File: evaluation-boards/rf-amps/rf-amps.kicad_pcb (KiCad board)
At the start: 4 copper layers, 23 x 37 mm, 22 parts, among them J1 Conn_01x02, J2 Conn_01x02, J3 CONN_01X03, J4 CONN_COAXIAL, J5 CONN_COAXIAL, J6 CONN_COAXIAL, J7 CONN_COAXIAL, U1 BGB741L7ESD

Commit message: Update rf-amps board
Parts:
- removed C5, C6: 100nF, gsg-modules:0402
- removed C7, C8: 1uF, gsg-modules:0603
- removed J6, J7: CONN_COAXIAL, gsg-modules:SMA-73251-2120
- C1, C2, C9: value 100nF -> 1uF; footprint gsg-modules:0402 -> Capacitor_SMD:C_0201_0603Metric
- C3, C4: footprint gsg-modules:0603 -> Capacitor_SMD:C_0201_0603Metric
- J4, J5: footprint gsg-modules:SMA-73251-2120 -> sma-variants:Linx_SMA_CONSMA003.062
- L1, L2: value 10uH -> 47uH; footprint gsg-modules:0603 -> Inductor_SMD:L_0603_1608Metric
- L3, L4: value 10uH -> 33nH; footprint gsg-modules:0603 -> Inductor_SMD:L_0201_0603Metric
- R1: footprint gsg-modules:0603 -> Resistor_SMD:R_0402_1005Metric
- moved L4 16.9 mm to (145.1, 80.3)
- moved L3 15.7 mm to (138.5, 79.7)
- moved C4 8.54 mm to (141.3, 81.3)
- moved L2 4.36 mm to (143.2, 81.3), turned to 180 degrees
- moved L1 4.11 mm to (138.4, 78.2), turned to 0 degrees
- moved C1 3.16 mm to (137.1, 80.0)
- moved C2 3.16 mm to (146.5, 80.0)
- moved J1 3.16 mm to (138.0, 67.6)
- moved J2 3.16 mm to (132.9, 67.6)
- moved J3 3.16 mm to (143.1, 67.6)
- moved J4 3.16 mm to (130.0, 80.0)
- moved J5 3.16 mm to (153.0, 80.0)
- moved R1 3.11 mm to (143.9, 77.3)
- moved U1 3.04 mm to (142.0, 79.5)
- moved C9 2.21 mm to (141.4, 78.3), turned to 180 degrees
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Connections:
- C1 pad 1: Net-(C1-Pad1) -> Net-(U1-RFIN)
- C2 pad 2: Net-(C2-Pad2) -> Net-(U1-RFOUT)
- L1 pad 1: Net-(C1-Pad1) -> Net-(L1-Pad1)
- L2 pad 1: Net-(C2-Pad2) -> Net-(L2-Pad1)
- L3 pad 1: Net-(C5-Pad1) -> Net-(U1-RFIN)
- L3 pad 2: Net-(C7-Pad2) -> Net-(L1-Pad1)
- L4 pad 1: Net-(C5-Pad1) -> Net-(U1-RFOUT)
- L4 pad 2: VCC -> Net-(L2-Pad1)
- U1 pad 3: Net-(C1-Pad1) -> Net-(U1-RFIN)
- U1 pad 4: Net-(C2-Pad2) -> Net-(U1-RFOUT)
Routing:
- net Net-(C5-Pad1): track 8.83 -> 0.00 mm
- net VCC: track 9.74 -> 3.57 mm, vias 4 -> 3
- net Net-(C5-Pad2): track 4.37 -> 0.00 mm
- net GND: track 6.49 -> 2.41 mm, vias 5 -> 3
- net Net-(C6-Pad1): track 3.87 -> 0.00 mm
- net Net-(C1-Pad1): track 3.70 -> 0.00 mm
- net Net-(C2-Pad2): track 3.50 -> 0.00 mm
- net Net-(U1-RFIN): track 0.00 -> 3.40 mm
- net Net-(U1-RFOUT): track 0.00 -> 3.00 mm
- net Net-(U1-BIAS): track 4.04 -> 2.21 mm
- net Net-(C7-Pad2): track 1.75 -> 0.00 mm
- net Net-(L1-Pad1): track 0.00 -> 1.55 mm
- net Net-(L2-Pad1): track 0.00 -> 1.39 mm
- net Net-(J3-Pin_2): track 12.8 -> 13.5 mm
- net Net-(U1-ADJ): track 2.40 -> 1.87 mm
- added copper zone on In1.Cu, net GND
- added copper zone on In2.Cu, net VCC
- removed copper zone on C2.Cu, net GND
- removed copper zone on C3.Cu, net VCC
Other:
- net class Default removed
- board text added: "2024-11-04"
- board text added: "IN"
- board text added: "OUT"
- board text added: "rf-amps"
- board text removed: "12 August 2020"
- board text removed: "J4 IN"
- board text removed: "J5 OUT"

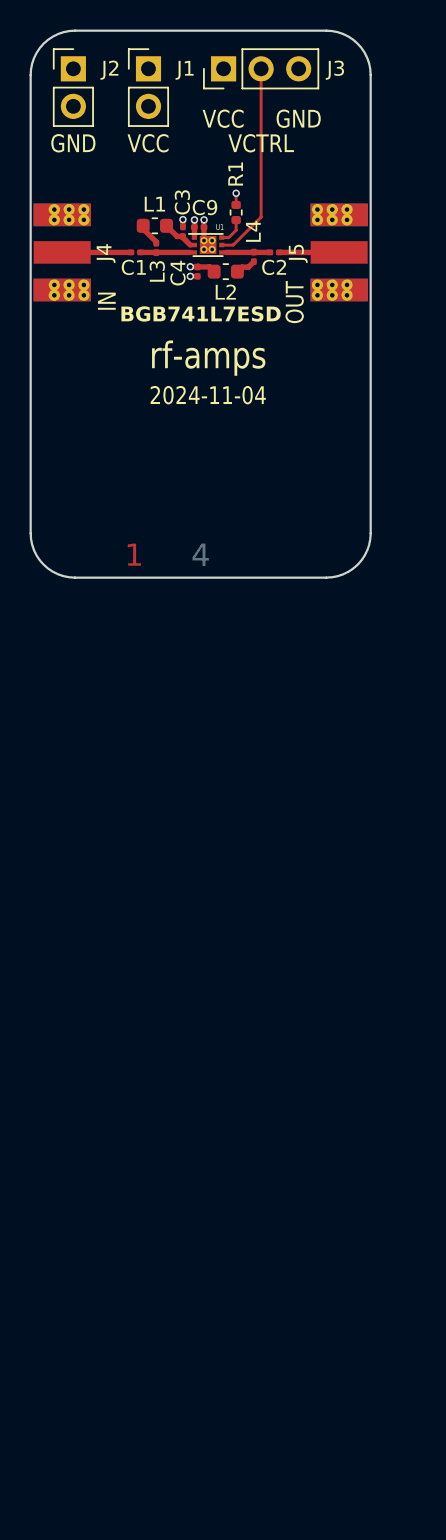
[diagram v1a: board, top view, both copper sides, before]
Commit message: Add more amplifiers to rf-amps board
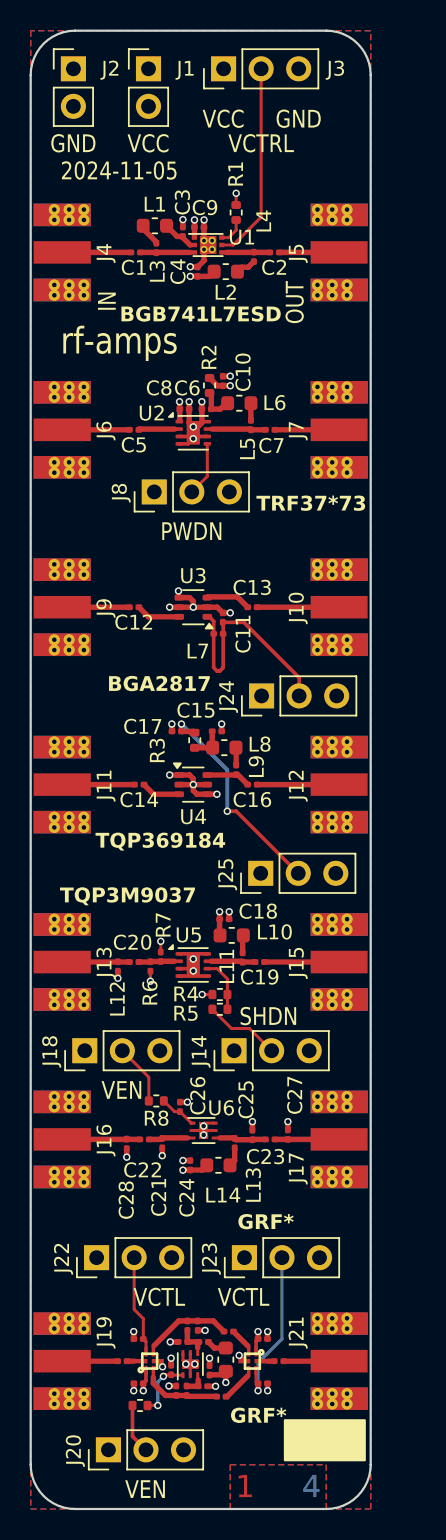
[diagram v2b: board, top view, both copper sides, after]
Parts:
- added C10: 1uF, Capacitor_SMD:C_0201_0603Metric, F.Cu at (143.0, 88.7)
- added C11: 1uF, Capacitor_SMD:C_0201_0603Metric, F.Cu at (143.0, 104.7)
- added C12: 1uF, Capacitor_SMD:C_0201_0603Metric, F.Cu at (137.0, 104.0)
- added C13: 1uF, Capacitor_SMD:C_0201_0603Metric, F.Cu at (145.0, 104.0)
- added C14: 1uF, Capacitor_SMD:C_0201_0603Metric, F.Cu at (137.3, 116.0)
- added C15: 1uF, Capacitor_SMD:C_0201_0603Metric, F.Cu at (142.6, 112.4)
- added C16: 1uF, Capacitor_SMD:C_0201_0603Metric, F.Cu at (145.0, 116.0)
- added C17: 1uF, Capacitor_SMD:C_0201_0603Metric, F.Cu at (139.9, 112.4)
- added C18: 1uF, Capacitor_SMD:C_0201_0603Metric, F.Cu at (143.1, 125.1)
- added C19: 1uF, Capacitor_SMD:C_0201_0603Metric, F.Cu at (145.5, 128.0)
- added C20: 1uF, Capacitor_SMD:C_0201_0603Metric, F.Cu at (137.0, 128.0)
- added C21: 0.2pF, Capacitor_SMD:C_0201_0603Metric, F.Cu at (138.9, 140.2)
- added C22: 1uF, Capacitor_SMD:C_0201_0603Metric, F.Cu at (137.7, 140.0)
- added C23: 1uF, Capacitor_SMD:C_0201_0603Metric, F.Cu at (146.2, 140.0)
- added C24: 1uF, Capacitor_SMD:C_0201_0603Metric, F.Cu at (140.8, 141.8)
- added C25: C, Capacitor_SMD:C_0201_0603Metric, F.Cu at (145.0, 139.7)
- added C26: 100pF, Capacitor_SMD:C_0201_0603Metric, F.Cu at (140.1, 137.8)
- added C27: C, Capacitor_SMD:C_0201_0603Metric, F.Cu at (147.4, 139.7)
- added C28: C, Capacitor_SMD:C_0201_0603Metric, F.Cu at (136.5, 140.3)
- added C29: C, Capacitor_SMD:C_0201_0603Metric, F.Cu at (139.8, 157.0)
- added C30: 1uF, Capacitor_SMD:C_0201_0603Metric, F.Cu at (140.6, 157.0)
- added C31: 0.2pF, Capacitor_SMD:C_0201_0603Metric, F.Cu at (141.7, 156.7)
- added C32: 100pF, Capacitor_SMD:C_0201_0603Metric, F.Cu at (139.5, 155.6)
- added C33: C, Capacitor_SMD:C_0201_0603Metric, F.Cu at (140.3, 153.7)
- added C34: 1uF, Capacitor_SMD:C_0201_0603Metric, F.Cu at (142.1, 155.6)
- added C35: 1uF, Capacitor_SMD:C_0201_0603Metric, F.Cu at (140.6, 152.6)
- added C36: C, Capacitor_SMD:C_0201_0603Metric, F.Cu at (141.3, 152.6)
- added C37: 1uF, Capacitor_SMD:C_0201_0603Metric, F.Cu at (136.2, 155.0)
- added C38: 1uF, Capacitor_SMD:C_0201_0603Metric, F.Cu at (146.8, 155.0)
- added C39: 1uF, Capacitor_SMD:C_0201_0603Metric, F.Cu at (142.9, 157.4)
- added C40: 1uF, Capacitor_SMD:C_0201_0603Metric, F.Cu at (143.4, 153.0)
- added C41: 1uF, Capacitor_SMD:C_0201_0603Metric, F.Cu at (137.3, 156.5)
- added C42: 1uF, Capacitor_SMD:C_0201_0603Metric, F.Cu at (145.7, 153.5)
- added C43: 1uF, Capacitor_SMD:C_0201_0603Metric, F.Cu at (137.3, 153.5)
- added C44: 1uF, Capacitor_SMD:C_0201_0603Metric, F.Cu at (145.7, 156.5)
- added C5: 1uF, Capacitor_SMD:C_0201_0603Metric, F.Cu at (137.0, 92.0)
- added C6: 1uF, Capacitor_SMD:C_0201_0603Metric, F.Cu at (141.9, 90.6)
- added C7: 1uF, Capacitor_SMD:C_0201_0603Metric, F.Cu at (146.2, 92.0)
- added C8: 1uF, Capacitor_SMD:C_0201_0603Metric, F.Cu at (140.4, 90.6)
- added J10: CONN_COAXIAL, sma-variants:Linx_SMA_CONSMA003.062, F.Cu at (153.0, 104.0)
- added J11: CONN_COAXIAL, sma-variants:Linx_SMA_CONSMA003.062, F.Cu at (130.0, 116.0)
- added J12: CONN_COAXIAL, sma-variants:Linx_SMA_CONSMA003.062, F.Cu at (153.0, 116.0)
- added J13: CONN_COAXIAL, sma-variants:Linx_SMA_CONSMA003.062, F.Cu at (130.0, 128.0)
- added J14: CONN_01X03, Connector_PinHeader_2.54mm:PinHeader_1x03_P2.54mm_Vertical, F.Cu at (143.8, 134.0)
- added J15: CONN_COAXIAL, sma-variants:Linx_SMA_CONSMA003.062, F.Cu at (153.0, 128.0)
- added J16: CONN_COAXIAL, sma-variants:Linx_SMA_CONSMA003.062, F.Cu at (130.0, 140.0)
- added J17: CONN_COAXIAL, sma-variants:Linx_SMA_CONSMA003.062, F.Cu at (153.0, 140.0)
- added J18: CONN_01X03, Connector_PinHeader_2.54mm:PinHeader_1x03_P2.54mm_Vertical, F.Cu at (133.7, 134.0)
- added J19: CONN_COAXIAL, sma-variants:Linx_SMA_CONSMA003.062, F.Cu at (130.0, 155.0)
- added J20: CONN_01X03, Connector_PinHeader_2.54mm:PinHeader_1x03_P2.54mm_Vertical, F.Cu at (135.3, 161.0)
- added J21: CONN_COAXIAL, sma-variants:Linx_SMA_CONSMA003.062, F.Cu at (153.0, 155.0)
- added J22: CONN_01X03, Connector_PinHeader_2.54mm:PinHeader_1x03_P2.54mm_Vertical, F.Cu at (134.5, 148.0)
- added J23: CONN_01X03, Connector_PinHeader_2.54mm:PinHeader_1x03_P2.54mm_Vertical, F.Cu at (144.5, 148.0)
- added J24: CONN_01X03, Connector_PinHeader_2.54mm:PinHeader_1x03_P2.54mm_Vertical, F.Cu at (145.6, 110.0)
- added J25: CONN_01X03, Connector_PinHeader_2.54mm:PinHeader_1x03_P2.54mm_Vertical, F.Cu at (145.6, 122.0)
- added J6: CONN_COAXIAL, sma-variants:Linx_SMA_CONSMA003.062, F.Cu at (130.0, 92.0)
- added J7: CONN_COAXIAL, sma-variants:Linx_SMA_CONSMA003.062, F.Cu at (153.0, 92.0)
- added J8: CONN_01X03, Connector_PinHeader_2.54mm:PinHeader_1x03_P2.54mm_Vertical, F.Cu at (138.4, 96.2)
- added J9: CONN_COAXIAL, sma-variants:Linx_SMA_CONSMA003.062, F.Cu at (130.0, 104.0)
- added L10: 33nH, Inductor_SMD:L_0201_0603Metric, F.Cu at (144.3, 127.7)
- added L11: 47uH, Inductor_SMD:L_0603_1608Metric, F.Cu at (143.6, 126.2)
- added L12: L, Inductor_SMD:L_0201_0603Metric, F.Cu at (135.9, 128.3)
- added L13: 33nH, Inductor_SMD:L_0201_0603Metric, F.Cu at (143.8, 140.2)
- added L14: 47uH, Inductor_SMD:L_0603_1608Metric, F.Cu at (142.7, 141.8)
- added L15: 33nH, Inductor_SMD:L_0201_0603Metric, F.Cu at (141.7, 153.7)
- added L16: 47uH, Inductor_SMD:L_0603_1608Metric, F.Cu at (143.2, 154.9)
- added L5: 33nH, Inductor_SMD:L_0201_0603Metric, F.Cu at (144.9, 91.7)
- added L6: 47uH, Inductor_SMD:L_0603_1608Metric, F.Cu at (144.1, 90.2)
- added L7: L, Inductor_SMD:L_0201_0603Metric, F.Cu at (142.7, 105.8)
- added L8: 33nH, Inductor_SMD:L_0201_0603Metric, F.Cu at (143.9, 115.0)
- added L9: 47uH, Inductor_SMD:L_0603_1608Metric, F.Cu at (143.1, 113.5)
- added R2: 0, Resistor_SMD:R_0402_1005Metric, F.Cu at (142.1, 89.0)
- added R3: 24, Resistor_SMD:R_0402_1005Metric, F.Cu at (141.1, 113.0)
- added R4: 10k, Resistor_SMD:R_0402_1005Metric, F.Cu at (142.8, 130.2)
- added R5: 33k, Resistor_SMD:R_0402_1005Metric, F.Cu at (142.8, 131.2)
- added R6: R, Resistor_SMD:R_0201_0603Metric, F.Cu at (138.1, 128.3)
- added R7: R, Resistor_SMD:R_0201_0603Metric, F.Cu at (138.8, 127.6)
- added R8: 900, Resistor_SMD:R_0402_1005Metric, F.Cu at (138.5, 137.4)
- added R9: 900, Resistor_SMD:R_0402_1005Metric, F.Cu at (137.4, 158.0)
- added U10: SKY13453, gsg-modules:SKY13350-385LF, F.Cu at (138.1, 155.0)
- added U2: TRF37A73, Package_SON:WSON-8-1EP_2x2mm_P0.5mm_EP0.9x1.6mm, F.Cu at (141.0, 92.2)
- added U3: BGA2817, Package_TO_SOT_SMD:SOT-363_SC-70-6, F.Cu at (141.0, 104.0)
- added U4: TQP369184, Package_TO_SOT_SMD:SOT-363_SC-70-6, F.Cu at (141.0, 116.0)
- added U5: TQP3M9037, Package_SON:WSON-8-1EP_2x2mm_P0.5mm_EP0.9x1.6mm, F.Cu at (141.0, 128.2)
- added U6: GRF4001, rf-amps:DFN-6-1EP_1.5x1.5mm_P0.5mm_EP0.6x1.1mm, F.Cu at (141.7, 139.4)
- added U7: SKY13453, gsg-modules:SKY13350-385LF, F.Cu at (145.0, 155.0)
- added U8: GRF4001, rf-amps:DFN-6-1EP_1.5x1.5mm_P0.5mm_EP0.6x1.1mm, F.Cu at (140.8, 155.2)
- turned C4 to -90 degrees
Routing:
- net GND: track 2.41 -> 45.9 mm, vias 3 -> 45
- net Net-(J24-Pin_2): track 0.00 -> 15.5 mm
- net Net-(J25-Pin_2): track 0.00 -> 15.2 mm, vias 0 -> 2
- net VCC: track 3.57 -> 15.3 mm, vias 3 -> 11
- net Net-(J23-Pin_2): track 0.00 -> 11.1 mm, vias 0 -> 1
- net Net-(J22-Pin_2): track 0.00 -> 6.69 mm
- net Net-(U10-RF2): track 0.00 -> 5.73 mm
- net Net-(J12-In): track 0.00 -> 5.55 mm
- net Net-(J10-In): track 0.00 -> 5.55 mm
- net Net-(J16-In): track 0.00 -> 5.26 mm
- net Net-(J14-Pin_2): track 0.00 -> 5.17 mm
- net Net-(U10-RF1): track 0.00 -> 5.06 mm
- net Net-(J15-In): track 0.00 -> 5.05 mm
- net Net-(J11-In): track 0.00 -> 4.89 mm
- net Net-(J13-In): track 0.00 -> 4.56 mm
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- added copper zone on B.Cu, net GND
- added copper zone on F.Cu, net GND
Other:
- board size 23 x 37 mm -> 23 x 100 mm
- board text added: "2024-11-05"
- board text added: "BGA2817"
- board text added: "GRF*"
- board text added: "PWDN"
- board text added: "SHDN"
- board text added: "TQP369184"
- board text added: "TQP3M9037"
- board text added: "TRF37*73"
- board text added: "VCTL"
- board text added: "VEN"
- board text removed: "2024-11-04"

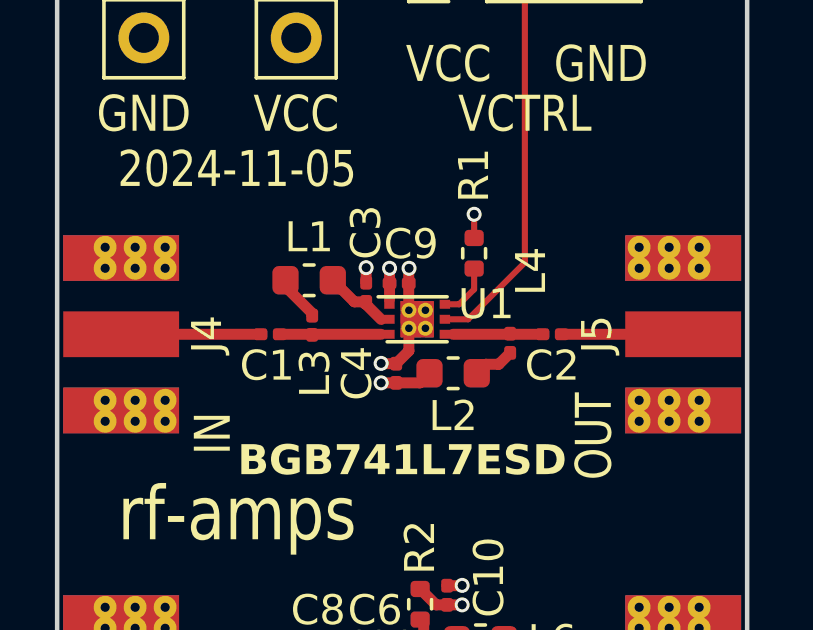
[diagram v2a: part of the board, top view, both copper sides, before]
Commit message: Update TSLP-7-1 footprint
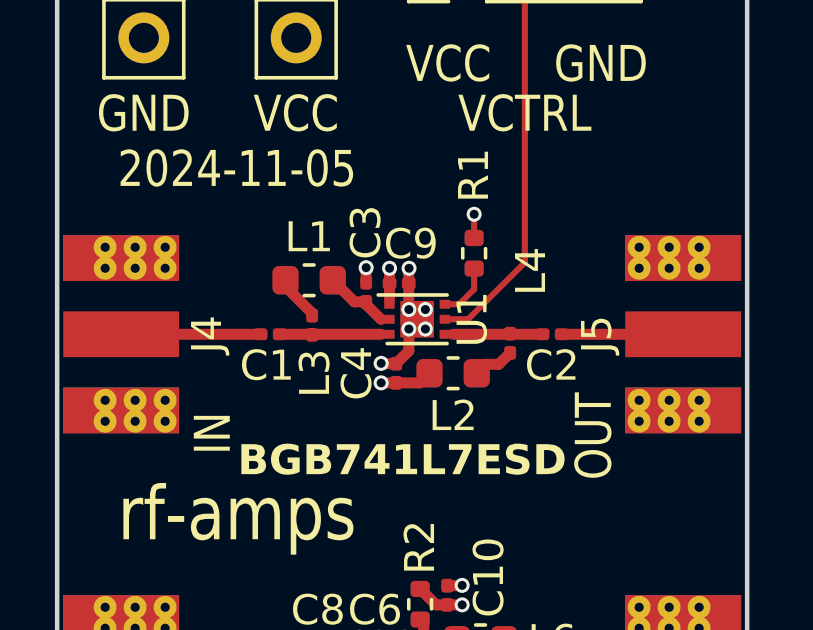
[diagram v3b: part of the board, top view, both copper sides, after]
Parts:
- U1: footprint gsg-modules:TSLP-7-1 -> rf-amps:TSLP-7-1
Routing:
- net GND: vias 45 -> 49

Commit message: Update rf-amps board
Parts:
- removed C11, C12, C13, C15, C3, C39, C42: 1uF, Capacitor_SMD:C_0201_0603Metric
- removed J20, J23: CONN_01X03, Connector_PinHeader_2.54mm:PinHeader_1x03_P2.54mm_Vertical
- removed L1, L14, L16, L2, L6, L9: 47uH, Inductor_SMD:L_0603_1608Metric
- removed L15, L4, L5: 33nH, Inductor_SMD:L_0201_0603Metric
- removed L7: L, Inductor_SMD:L_0201_0603Metric
- removed U10, U7: SKY13453, gsg-modules:SKY13350-385LF
- removed the U3 at (141.0, 104.0)
- removed U5: TQP3M9037, Package_SON:WSON-8-1EP_2x2mm_P0.5mm_EP0.9x1.6mm
- removed U6, U8: GRF4001, rf-amps:DFN-6-1EP_1.5x1.5mm_P0.5mm_EP0.6x1.1mm
- added C45: 39pF, Capacitor_SMD:C_0201_0603Metric, F.Cu at (142.9, 112.6)
- added C46: 39pF, Capacitor_SMD:C_0201_0603Metric, F.Cu at (138.9, 125.2)
- added C47: 39pF, Capacitor_SMD:C_0201_0603Metric, F.Cu at (142.1, 135.8)
- added C48: 39pF, Capacitor_SMD:C_0201_0603Metric, F.Cu at (140.3, 155.7)
- added C49: C, Capacitor_SMD:C_0201_0603Metric, F.Cu at (144.5, 124.6)
- added C50: C, Capacitor_SMD:C_0201_0603Metric, F.Cu at (145.2, 154.4)
- added C53: C, Capacitor_SMD:C_0201_0603Metric, F.Cu at (141.7, 104.8)
- added C54: C, Capacitor_SMD:C_0201_0603Metric, F.Cu at (143.8, 102.6)
- added C55: 1uF, Capacitor_SMD:C_0201_0603Metric, F.Cu at (146.2, 99.7)
- added C56: C, Capacitor_SMD:C_0201_0603Metric, F.Cu at (138.5, 102.3)
- added L17: 47uH, Inductor_SMD:L_0603_1608Metric, F.Cu at (142.7, 125.5)
- added L18: 33nH, Inductor_SMD:L_0201_0603Metric, F.Cu at (142.3, 127.7)
- added L19: 47uH, Inductor_SMD:L_0603_1608Metric, F.Cu at (143.4, 153.5)
- added L20: 33nH, Inductor_SMD:L_0201_0603Metric, F.Cu at (143.0, 151.3)
- added L23: 47uH, Inductor_SMD:L_0603_1608Metric, F.Cu at (144.3, 101.5)
- added L24: 33nH, Inductor_SMD:L_0201_0603Metric, F.Cu at (143.5, 103.7)
- added L25: L, Inductor_SMD:L_0201_0603Metric, F.Cu at (135.9, 139.6)
- added L26: L, Inductor_SMD:L_0201_0603Metric, F.Cu at (137.2, 153.2)
- added L27: L, Inductor_SMD:L_0201_0603Metric, F.Cu at (137.9, 128.3)
- added Q1: BFR840, eval:TSLP-3-9, F.Cu at (141.5, 115.7)
- added Q2: BFR840, eval:TSLP-3-9, F.Cu at (141.5, 127.7)
- added Q3: BFP840ESD, eval:SOT-343-4-3, F.Cu at (140.9, 140.0)
- added Q4: BFP840ESD, eval:SOT-343-4-3, F.Cu at (141.5, 152.0)
- added R11: R, Resistor_SMD:R_0201_0603Metric, F.Cu at (144.2, 126.7)
- added R12: 33k, Resistor_SMD:R_0201_0603Metric, F.Cu at (140.0, 127.7)
- added R13: 27, Resistor_SMD:R_0201_0603Metric, F.Cu at (141.2, 125.2)
- added R14: 0, Resistor_SMD:R_0201_0603Metric, F.Cu at (141.2, 126.7)
- added R15: 0, Resistor_SMD:R_0201_0603Metric, F.Cu at (143.8, 124.6)
- added R16: 30k, Resistor_SMD:R_0201_0603Metric, F.Cu at (140.2, 136.1)
- added R17: 82, Resistor_SMD:R_0201_0603Metric, F.Cu at (141.8, 155.2)
- added R18: 82, Resistor_SMD:R_0201_0603Metric, F.Cu at (143.7, 136.7)
- added R19: 0, Resistor_SMD:R_0201_0603Metric, F.Cu at (143.1, 78.5)
- added R20: 10, Resistor_SMD:R_0201_0603Metric, F.Cu at (144.5, 141.0)
- added R21: 30k, Resistor_SMD:R_0201_0603Metric, F.Cu at (140.3, 155.0)
- added R22: 82, Resistor_SMD:R_0201_0603Metric, F.Cu at (141.8, 154.4)
- added R23: 10, Resistor_SMD:R_0201_0603Metric, F.Cu at (143.7, 150.6)
- added R24: 0, Resistor_SMD:R_0201_0603Metric, F.Cu at (141.8, 153.8)
- added R25: R, Resistor_SMD:R_0201_0603Metric, F.Cu at (144.8, 152.3)
- added R26: 0, Resistor_SMD:R_0201_0603Metric, F.Cu at (144.5, 154.4)
- added R36: R, Resistor_SMD:R_0201_0603Metric, F.Cu at (140.3, 104.8)
- added R37: R, Resistor_SMD:R_0201_0603Metric, F.Cu at (145.3, 102.6)
- added R38: 0, Resistor_SMD:R_0201_0603Metric, F.Cu at (145.1, 100.0)
- added R39: 0, Resistor_SMD:R_0201_0603Metric, F.Cu at (144.6, 104.0)
- added R40: 0, Resistor_SMD:R_0201_0603Metric, F.Cu at (140.0, 150.7)
- added R45: 0, Resistor_SMD:R_0201_0603Metric, F.Cu at (145.2, 141.0)
- added R46: 0, Resistor_SMD:R_0201_0603Metric, F.Cu at (144.4, 150.6)
- added R47: 0, Resistor_SMD:R_0201_0603Metric, F.Cu at (143.7, 128.4)
- added R48: 0, Resistor_SMD:R_0201_0603Metric, F.Cu at (143.0, 128.4)
- C18, C23, C30: value 1uF -> 1pF
- C19, C24: value 1uF -> 18pF
- C20, C22: value 1uF -> 22pF
- C21: value 0.2pF -> 1uF
- C26: value 100pF -> C
- C27, C33: value C -> 1uF
- C28: value C -> 39pF
- C29: value C -> 3.3pF
- C31: value 0.2pF -> 10pF
- C32: value 100pF -> 10pF
- C34: value 1uF -> 39pF
- C35: value 1uF -> 3.3pF
- C36: value C -> 1pF
- C37, C38: value 1uF -> 10pF
- C4, C40, C41, C43, C44, C6: value 1uF -> C
- L10: value 33nH -> 3.7nH
- L11: value 47uH -> 2.2nH; footprint Inductor_SMD:L_0603_1608Metric -> Inductor_SMD:L_0201_0603Metric
- L12: value L -> 5.1nH
- L13: value 33nH -> 5.1nH
- L3: value 33nH -> 4.7 nH
- L8: value 33nH -> L
- P3: renamed from J3; value CONN_01X03 -> CONN_02X03; footprint Connector_PinHeader_2.54mm:PinHeader_1x03_P2.54mm_Vertical -> Connector_PinHeader_2.54mm:PinHeader_2x03_P2.54mm_Vertical
- P4: renamed from J8; value CONN_01X03 -> CONN_02X03; footprint Connector_PinHeader_2.54mm:PinHeader_1x03_P2.54mm_Vertical -> Connector_PinHeader_2.54mm:PinHeader_2x03_P2.54mm_Vertical
- R1: value 3k -> 0; footprint Resistor_SMD:R_0402_1005Metric -> Resistor_SMD:R_0201_0603Metric
- R2: value 0 -> R; footprint Resistor_SMD:R_0402_1005Metric -> Resistor_SMD:R_0201_0603Metric
- R3: value 24 -> 33k; footprint Resistor_SMD:R_0402_1005Metric -> Resistor_SMD:R_0201_0603Metric
- R4: value 10k -> 120; footprint Resistor_SMD:R_0402_1005Metric -> Resistor_SMD:R_0201_0603Metric
- R5: value 33k -> 27; footprint Resistor_SMD:R_0402_1005Metric -> Resistor_SMD:R_0201_0603Metric
- R6: value R -> 0
- R7: value R -> 120
- R8: value 900 -> 0; footprint Resistor_SMD:R_0402_1005Metric -> Resistor_SMD:R_0201_0603Metric
- R9: value 900 -> 82; footprint Resistor_SMD:R_0402_1005Metric -> Resistor_SMD:R_0201_0603Metric
- U1: value BGB741L7ESD -> BGA9H1BN6; footprint rf-amps:TSLP-7-1 -> eval:TSLP-6-4_1.1x0.7mm_P0.4mm
- U2: value TRF37A73 -> BGA8U1BN6; footprint Package_SON:WSON-8-1EP_2x2mm_P0.5mm_EP0.9x1.6mm -> eval:TSLP-6-4_1.1x0.7mm_P0.4mm
- U3: renamed from U4; value TQP369184 -> BGB741L7ESD; footprint Package_TO_SOT_SMD:SOT-363_SC-70-6 -> rf-amps:TSLP-7-1
- moved C6 61.1 mm to (144.1, 151.7)
- moved C4 46.1 mm to (143.3, 127.3), turned to 0 degrees
- moved C44 28.2 mm to (145.8, 128.3), turned to -90 degrees
- moved C25 25.6 mm to (140.0, 114.6), turned to 0 degrees
- moved C43 25.4 mm to (140.7, 128.3), turned to -90 degrees
- moved R9 24.5 mm to (143.7, 134.3), turned to -90 degrees
- moved R4 20.0 mm to (142.8, 110.2), turned to -90 degrees
- moved C30 18.9 mm to (144.0, 138.4), turned to 180 degrees
- moved R6 18.2 mm to (141.6, 110.5), turned to 180 degrees
- moved C29 17.9 mm to (136.9, 139.3), turned to 180 degrees
- moved P5 17.8 mm to (132.5, 98.0)
- moved P6 17.8 mm to (132.5, 110.0)
- moved R5 17.5 mm to (142.6, 113.7), turned to -90 degrees
- moved C32 17.2 mm to (147.3, 140.3), turned to 90 degrees
- moved C31 16.7 mm to (146.2, 140.7)
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- renumbered J4 to J1, J15 to J10, J16 to J11, J17 to J12, J19 to J13, J21 to J14, J5 to J2, J6 to J3, J7 to J4, J9 to J5, J10 to J6, J11 to J7, J12 to J8, J13 to J9, J2 to P1, J1 to P2, J24 to P5, J25 to P6, J14 to P7, J18 to P8, J22 to P9
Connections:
- C1 pad 1: Net-(U1-RFIN) -> Net-(C1-Pad1)
- C14 pad 1: Net-(C14-Pad1) -> Net-(U3-RFIN)
- C14 pad 2: Net-(J11-In) -> Net-(J5-In)
- C16 pad 1: Net-(J12-In) -> Net-(J6-In)
- C17 pad 1: GND -> Net-(P6-Pin_2)
- C17 pad 2: Net-(J25-Pin_2) -> GND
- C18 pad 2: VCC -> Net-(C18-Pad2)
- C19 pad 1: Net-(J15-In) -> Net-(J8-In)
- C19 pad 2: Net-(U5-RFOUT) -> Net-(Q1-C)
- C2 pad 2: Net-(U1-RFOUT) -> Net-(C2-Pad2)
- C20 pad 1: Net-(U5-RFIN) -> Net-(Q1-B)
- C20 pad 2: Net-(J13-In) -> Net-(J7-In)
- C21 pad 1: GND -> Net-(P7-Pin_2)
- C21 pad 2: Net-(U6-RFIN) -> GND
- C22 pad 1: Net-(U6-RFIN) -> Net-(Q2-B)
- C22 pad 2: Net-(J16-In) -> Net-(J9-In)
- C23 pad 1: Net-(J17-In) -> GND
- C23 pad 2: Net-(U6-RFOUT) -> Net-(C23-Pad2)
- C24 pad 1: GND -> Net-(J10-In)
- C24 pad 2: VCC -> Net-(C24-Pad2)
- C25 pad 1: Net-(U6-RFOUT) -> GND
- C25 pad 2: GND -> Net-(C25-Pad2)
- C27 pad 1: Net-(J17-In) -> Net-(P8-Pin_2)
- C28 pad 1: Net-(J16-In) -> GND
- C28 pad 2: GND -> Net-(C28-Pad2)
- C29 pad 1: Net-(U10-RF1) -> Net-(Q3-B)
- C29 pad 2: GND -> Net-(J11-In)
- C30 pad 1: Net-(U8-RFIN) -> GND
- C30 pad 2: Net-(U10-RF1) -> Net-(C30-Pad2)
- C31 pad 1: GND -> Net-(J12-In)
- C31 pad 2: Net-(U8-RFIN) -> Net-(C31-Pad2)
- C32 pad 1: GND -> Net-(J12-In)
- C32 pad 2: Net-(U8-VEN) -> GND
- C33 pad 1: Net-(U8-RFOUT) -> Net-(P9-Pin_2)
- C34 pad 2: VCC -> Net-(C34-Pad2)
- C35 pad 1: Net-(U10-RF2) -> Net-(Q4-B)
- C35 pad 2: Net-(U8-RFOUT) -> Net-(J13-In)
- C36 pad 1: Net-(U10-RF2) -> GND
- C36 pad 2: GND -> Net-(C36-Pad2)
- C37 pad 1: Net-(U10-RFC) -> Net-(J14-In)
- C37 pad 2: Net-(J19-In) -> Net-(C37-Pad2)
- C38 pad 1: Net-(J21-In) -> Net-(J14-In)
- C38 pad 2: Net-(U7-RFC) -> GND
- C4 pad 1: GND -> Net-(C4-Pad1)
- C4 pad 2: VCC -> Net-(C4-Pad2)
- C40 pad 1: Net-(U10-RF2) -> Net-(Q3-B)
- C40 pad 2: Net-(U7-RF1) -> GND
- C41 pad 1: GND -> Net-(Q4-B)
- C41 pad 2: VCC -> GND
- C43 pad 1: GND -> Net-(Q2-B)
- C43 pad 2: Net-(J22-Pin_2) -> GND
- C44 pad 1: GND -> Net-(J10-In)
- C44 pad 2: Net-(J23-Pin_2) -> GND
- C5 pad 1: Net-(U2-RFIN) -> Net-(C5-Pad1)
- C6 pad 1: GND -> Net-(C6-Pad1)
- C7 pad 2: Net-(U2-RFOUT) -> Net-(C7-Pad2)
- J10 pad 1: Net-(J15-In) -> Net-(J10-In)
- J11 pad 1: Net-(J16-In) -> Net-(J11-In)
- J12 pad 1: Net-(J17-In) -> Net-(J12-In)
- J13 pad 1: Net-(J19-In) -> Net-(J13-In)
- J14 pad 1: Net-(J21-In) -> Net-(J14-In)
- J5 pad 1: Net-(J9-In) -> Net-(J5-In)
- J6 pad 1: Net-(J10-In) -> Net-(J6-In)
- J7 pad 1: Net-(J11-In) -> Net-(J7-In)
- J8 pad 1: Net-(J12-In) -> Net-(J8-In)
- J9 pad 1: Net-(J13-In) -> Net-(J9-In)
- L10 pad 1: Net-(U5-RFOUT) -> Net-(C18-Pad2)
- L10 pad 2: Net-(L10-Pad2) -> Net-(Q1-C)
- L11 pad 1: Net-(L10-Pad2) -> Net-(C30-Pad2)
- L11 pad 2: VCC -> Net-(L11-Pad2)
- L12 pad 1: GND -> Net-(C28-Pad2)
- L12 pad 2: Net-(J13-In) -> Net-(Q3-B)
- L13 pad 1: Net-(U6-RFOUT) -> Net-(C34-Pad2)
- L13 pad 2: Net-(L13-Pad2) -> Net-(Q4-B)
- L3 pad 1: Net-(U1-RFIN) -> Net-(C1-Pad1)
- L3 pad 2: Net-(L1-Pad1) -> Net-(L3-Pad2)
- L8 pad 1: Net-(C16-Pad2) -> Net-(U3-RFIN)
- L8 pad 2: Net-(L8-Pad2) -> Net-(U3-BIAS)
- P3 pad 2: Net-(J3-Pin_2) -> VCC
- P3 pad 3: GND -> Net-(P3-Pin_3)
- P4 pad 2: Net-(J8-Pin_2) -> VCC
- P4 pad 3: GND -> Net-(P4-Pin_3)
- P5 pad 2: Net-(J24-Pin_2) -> Net-(P5-Pin_2)
- P6 pad 2: Net-(J25-Pin_2) -> Net-(P6-Pin_2)
- P7 pad 2: Net-(J14-Pin_2) -> Net-(P7-Pin_2)
- P8 pad 2: Net-(J18-Pin_2) -> Net-(P8-Pin_2)
- P9 pad 2: Net-(J22-Pin_2) -> Net-(P9-Pin_2)
- R1 pad 1: VCC -> Net-(U1-C2)
- R1 pad 2: Net-(U1-ADJ) -> GND
- R2 pad 1: Net-(C6-Pad2) -> VCC
- R2 pad 2: VCC -> Net-(U3-ADJ)
- R3 pad 1: Net-(C15-Pad2) -> Net-(C25-Pad2)
- R3 pad 2: Net-(J25-Pin_2) -> Net-(Q1-B)
- R4 pad 1: GND -> Net-(P6-Pin_2)
- R4 pad 2: Net-(U5-SHUTDOWN) -> Net-(C45-Pad1)
- R5 pad 1: Net-(J14-Pin_2) -> Net-(C45-Pad1)
- R5 pad 2: Net-(U5-SHUTDOWN) -> Net-(C18-Pad2)
- R6 pad 1: Net-(U5-RFIN) -> Net-(C45-Pad1)
- R6 pad 2: GND -> Net-(C25-Pad2)
- R7 pad 1: VCC -> Net-(P7-Pin_2)
- R7 pad 2: Net-(U5-RFIN) -> Net-(C46-Pad1)
- R8 pad 1: Net-(J18-Pin_2) -> Net-(C46-Pad1)
- R9 pad 1: Net-(J20-Pin_2) -> Net-(P8-Pin_2)
- R9 pad 2: Net-(U8-VEN) -> Net-(C47-Pad1)
- U1 pad 1: VCC -> GND
- U1 pad 2: Net-(U1-BIAS) -> VCC
- U1 pad 3: Net-(U1-RFIN) -> Net-(C2-Pad2)
- U1 pad 4: Net-(U1-RFOUT) -> Net-(U1-C2)
- U1 pad 5: Net-(J3-Pin_2) -> Net-(L3-Pad2)
- U1 pad 6: Net-(U1-ADJ) -> Net-(P3-Pin_4)
- U2 pad 1: VCC -> Net-(P4-Pin_3)
- U2 pad 2: Net-(U2-RFIN) -> VCC
- U2 pad 3: GND -> Net-(C7-Pad2)
- U2 pad 4: GND -> Net-(P4-Pin_4)
- U2 pad 5: Net-(J8-Pin_2) -> GND
- U2 pad 6: GND -> Net-(C5-Pad1)
- U3 pad 1: GND -> VCC
- U3 pad 2: GND -> Net-(U3-BIAS)
- U3 pad 3: Net-(C14-Pad1) -> Net-(U3-RFIN)
- U3 pad 4: GND -> Net-(U3-RFOUT)
- U3 pad 5: GND -> Net-(P5-Pin_2)
- U3 pad 6: Net-(C16-Pad2) -> Net-(U3-ADJ)
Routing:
- net Net-(P9-Pin_2): track 0.00 -> 20.0 mm, vias 0 -> 2
- net GND: track 45.9 -> 26.8 mm
- net Net-(P7-Pin_2): track 0.00 -> 16.7 mm
- net Net-(P3-Pin_4): track 0.00 -> 15.7 mm, vias 0 -> 1
- net Net-(J24-Pin_2): track 15.5 -> 0.00 mm
- net Net-(J25-Pin_2): track 15.2 -> 0.00 mm, vias 2 -> 0
- net Net-(J3-Pin_2): track 13.5 -> 0.00 mm
- net Net-(P5-Pin_2): track 0.00 -> 11.9 mm
- net Net-(J23-Pin_2): track 11.1 -> 0.00 mm, vias 1 -> 0
- net Net-(P8-Pin_2): track 0.00 -> 10.7 mm
- net Net-(P4-Pin_4): track 0.00 -> 9.95 mm
- net VCC: track 15.3 -> 5.68 mm, vias 11 -> 5
- net Net-(P6-Pin_2): track 0.00 -> 9.47 mm
- net Net-(P3-Pin_3): track 0.00 -> 9.32 mm
- net Net-(J7-In): track 0.00 -> 6.95 mm
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- removed copper zone on F.Cu, net GND
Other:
- rule pad_to_mask_clearance: 0.0762 -> 0.05
- board text added: "2025-04-11"
- board text added: "BFP840"
- board text added: "BFR840"
- board text added: "BGA8U1BN6"
- board text added: "BGA9H1BN6"
- board text added: "BGB741"
- board text added: "C1"
- board text added: "C2"
- board text removed: "2024-11-05"
- board text removed: "BGA2817"
- board text removed: "BGB741L7ESD"
- board text removed: "GRF*"
- board text removed: "PWDN"
- board text removed: "SHDN"
- board text removed: "TQP369184"
- board text removed: "TQP3M9037"
- board text removed: "TRF37*73"
- board text removed: "VCTL"
- board text removed: "VCTRL"
- board text removed: "VEN"
